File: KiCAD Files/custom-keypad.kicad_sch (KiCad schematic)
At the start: 134 parts, among them SW1 SW_Push, SW10 SW_Push, SW11 SW_Push, SW12 SW_Push, SW13 SW_Push, SW14 SW_Push, SW15 SW_Push, SW16 SW_Push, SW17 SW_Push, SW18 SW_Push, SW19 SW_Push, SW2 SW_Push, SW20 SW_Push, SW21 SW_Push, SW22 SW_Push, SW23 SW_Push, SW24 SW_Push, SW25 SW_Push, SW26 SW_Push, SW27 SW_Push, SW28 SW_Push, SW29 SW_Push, SW3 SW_Push, SW30 SW_Push, SW31 SW_Push, SW32 SW_Push, SW33 SW_Push, SW34 SW_Push, SW35 SW_Push, SW36 SW_Push, SW37 SW_Push, SW38 SW_Push, SW39 SW_Push, SW4 SW_Push, SW40 SW_Push, SW41 SW_Push, SW42 SW_Push, SW43 SW_Push, SW44 SW_Push, SW45 SW_Push, SW46 SW_Push, SW47 SW_Push, SW48 SW_Push, SW49 SW_Push, SW5 SW_Push, SW50 SW_Push, SW51 SW_Push, SW52 SW_Push, SW53 SW_Push, SW54 SW_Push, SW55 SW_Push, SW56 SW_Push, SW57 SW_Push, SW58 SW_Push, SW59 SW_Push, SW6 SW_Push, SW60 SW_Push, SW61 SW_Push, SW62 SW_Push, SW63 SW_Push, SW64 SW_Push, SW65 SW_Push, SW66 SW_Push, SW67 SW_Push, SW7 SW_Push, SW8 SW_Push, SW9 SW_Push

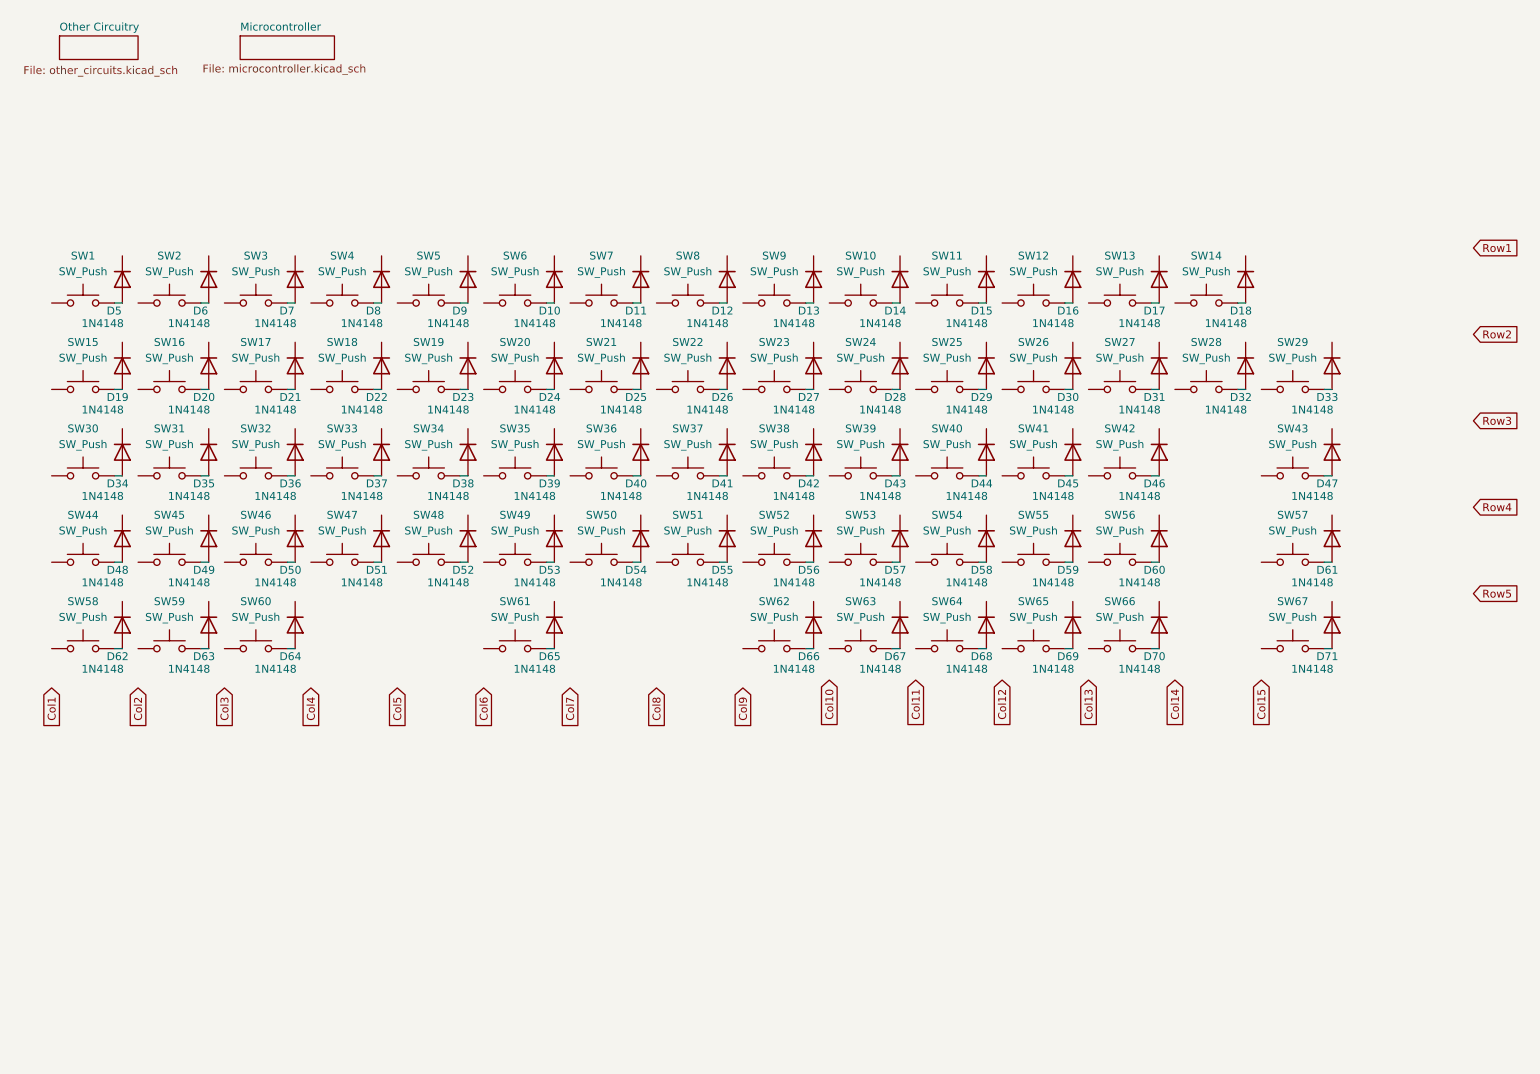
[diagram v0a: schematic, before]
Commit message: Revert "started adjusting changes for 65% keyboard"
This reverts commit 731512e8e337a2e6137dad3074b859df4f5567bd.
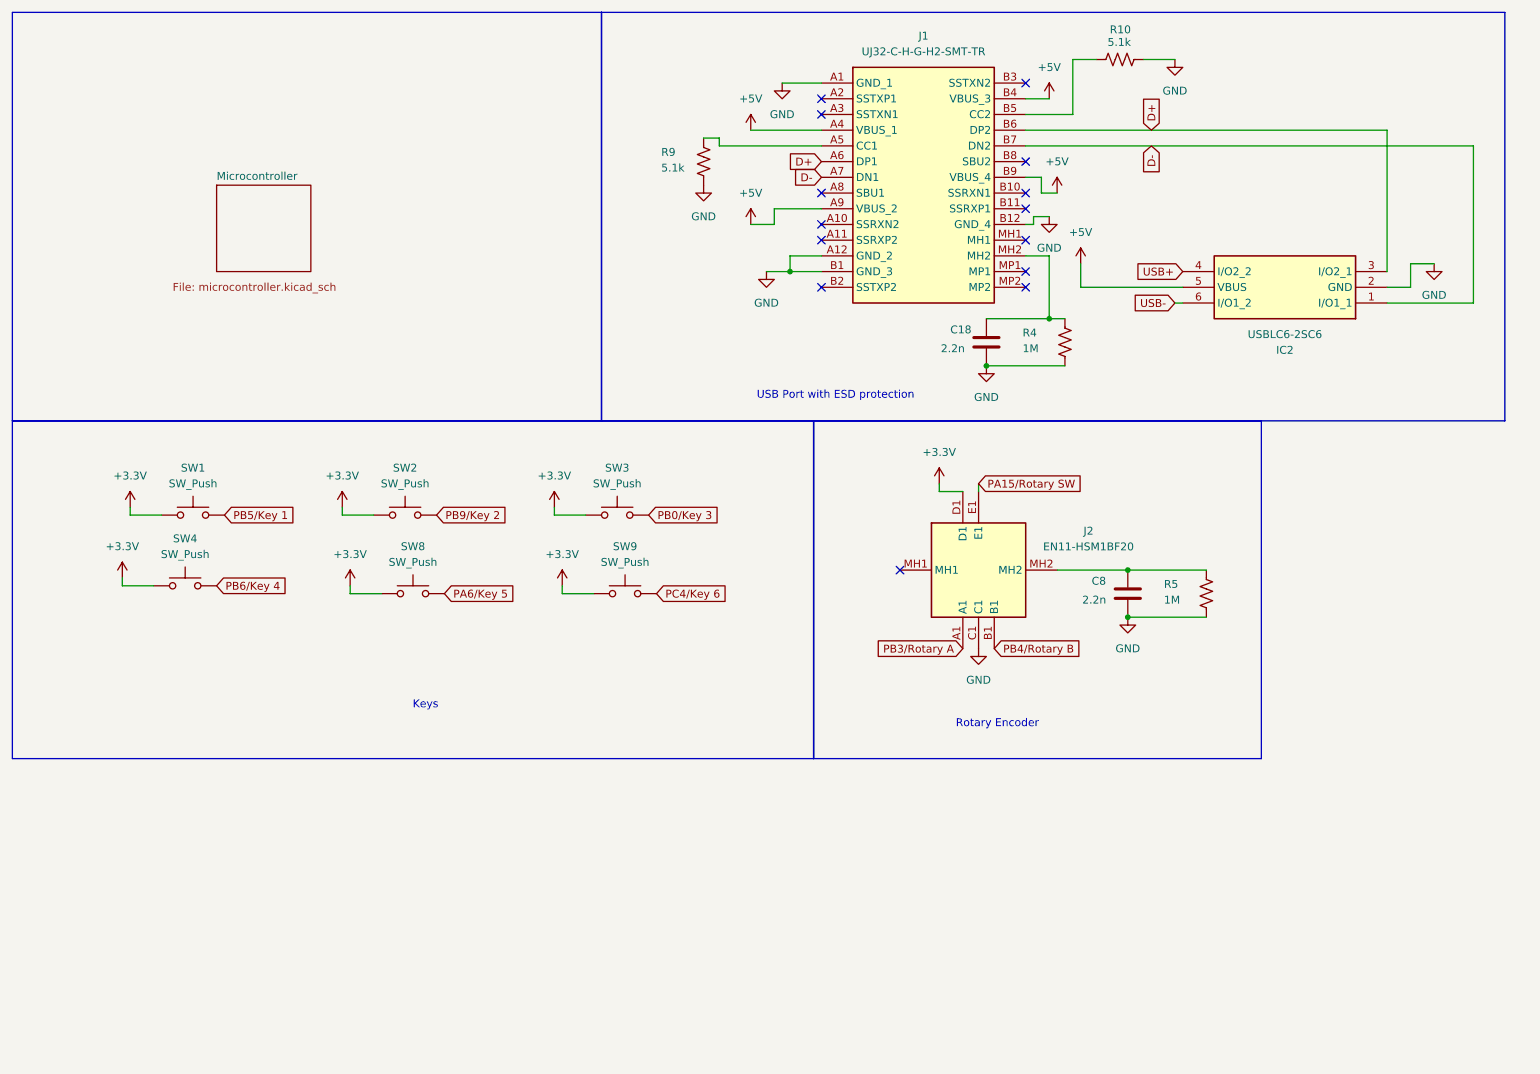
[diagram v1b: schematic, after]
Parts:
- removed D10, D11, D12, D13, D14, D15, D16, D17, D18, D19, D20, D21, D22, D23, D24, D25, D26, D27, D28, D29, D30, D31, D32, D33, D34, D35, D36, D37, D38, D39, D40, D41, D42, D43, D44, D45, D46, D47, D48, D49, D5, D50, D51, D52, D53, D54, D55, D56, D57, D58, D59, D6, D60, D61, D62, D63, D64, D65, D66, D67, D68, D69, D7, D70, D71, D8, D9: 1N4148, Diode_THT:D_DO-35_SOD27_P7.62mm_Horizontal, symbol Diode:1N4148
- removed SW10, SW11, SW12, SW13, SW14, SW15, SW16, SW17, SW18, SW19, SW20, SW21, SW22, SW23, SW24, SW25, SW26, SW27, SW28, SW29, SW30, SW31, SW32, SW33, SW34, SW35, SW36, SW37, SW38, SW39, SW40, SW41, SW42, SW43, SW44, SW45, SW46, SW47, SW48, SW49, SW5, SW50, SW51, SW52, SW53, SW54, SW55, SW56, SW57, SW58, SW59, SW6, SW60, SW61, SW62, SW63, SW64, SW65, SW66, SW67, SW7: SW_Push, symbol Switch:SW_Push
- added C18, C8: 2.2n, Capacitor_SMD:C_0805_2012Metric_Pad1.18x1.45mm_HandSolder, symbol CustomSymbols:C
- added IC2: USBLC6-2SC6, SOT95P280X145-6N, symbol CustomSymbols:USBLC6-2SC6
- added J1: UJ32-C-H-G-H2-SMT-TR, UJ32CHGH2SMTTR, symbol CustomSymbols:UJ32-C-H-G-H2-SMT-TR
- added J2: EN11-HSM1BF20, EN11HSM1BF20, symbol CustomSymbols:EN11-HSM1BF20
- added R10, R9: 5.1k, Resistor_SMD:R_0805_2012Metric_Pad1.20x1.40mm_HandSolder, symbol CustomSymbols:R_US
- added R4, R5: 1M, Resistor_SMD:R_0805_2012Metric_Pad1.20x1.40mm_HandSolder, symbol CustomSymbols:R_US
- SW1, SW2, SW3, SW4, SW8, SW9: footprint (none) -> CustomFootprints:SW_MX
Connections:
- net PC4/Key 6: now reaches SW9.2
- net +3.3V: now reaches SW1.1
- net +3.3V: now also SW2.1, SW3.1, SW4.1, SW8.1, SW9.1, J2.D1
- net PB5/Key 1: now reaches SW1.2
- net PA6/Key 5: now reaches SW8.2
- net PB6/Key 4: now reaches SW4.2
- net PB9/Key 2: now reaches SW2.2
- net PB0/Key 3: now reaches SW3.2
- new net: C18.1, J1.MH2, R4.1
- new net: C8.1, J2.MH2, R5.1
- new net: J1.A5 (CC1), R9.1
- new net: J1.B5 (CC2), R10.1
- new net +5V: IC2.5 (VBUS), J1.A4 (VBUS_1), J1.A9 (VBUS_2), J1.B4 (VBUS_3), J1.B9 (VBUS_4)
- new net D+: IC2.3 (I/O2_1), J1.A6 (DP1), J1.B6 (DP2)
- new net D-: IC2.1 (I/O1_1), J1.A7 (DN1), J1.B7 (DN2)
- new net GND: C18.2, C8.2, IC2.2 (GND), J1.A1 (GND_1), J1.A12 (GND_2), J1.B1 (GND_3), J1.B12 (GND_4), J2.C1, R10.2, R4.2, R5.2, R9.2
- new net PA15/Rotary SW: J2.E1
- new net PB3/Rotary A: J2.A1
- new net PB4/Rotary B: J2.B1
- new net USB+: IC2.4 (I/O2_2)
- new net USB-: IC2.6 (I/O1_2)
- no-connect marks 0 -> 14
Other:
- removed sheet Other Circuitry
- note added: "Keys"
- note added: "Rotary Encoder"
- note added: "USB Port with ESD protection"

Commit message: updated with keyboard 65%
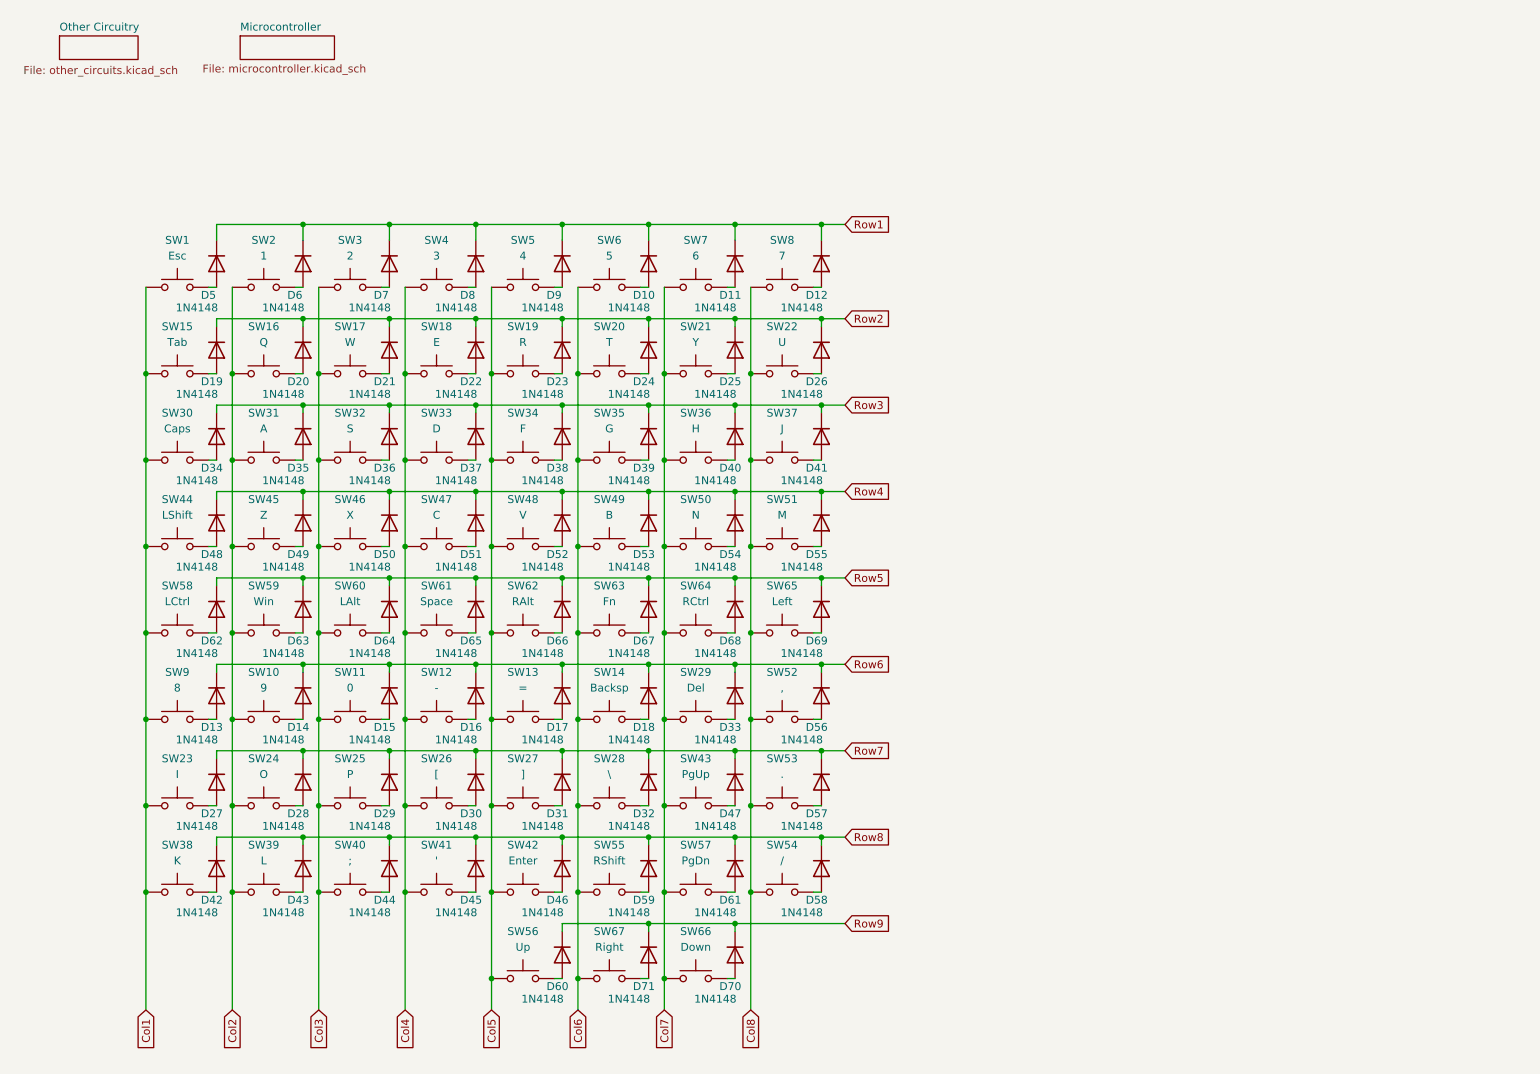
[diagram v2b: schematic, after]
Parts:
- removed C18, C8: 2.2n, Capacitor_SMD:C_0805_2012Metric_Pad1.18x1.45mm_HandSolder, symbol CustomSymbols:C
- removed IC2: USBLC6-2SC6, SOT95P280X145-6N, symbol CustomSymbols:USBLC6-2SC6
- removed J1: UJ32-C-H-G-H2-SMT-TR, UJ32CHGH2SMTTR, symbol CustomSymbols:UJ32-C-H-G-H2-SMT-TR
- removed J2: EN11-HSM1BF20, EN11HSM1BF20, symbol CustomSymbols:EN11-HSM1BF20
- removed R10, R9: 5.1k, Resistor_SMD:R_0805_2012Metric_Pad1.20x1.40mm_HandSolder, symbol CustomSymbols:R_US
- removed R4, R5: 1M, Resistor_SMD:R_0805_2012Metric_Pad1.20x1.40mm_HandSolder, symbol CustomSymbols:R_US
- added D10, D11, D12, D13, D14, D15, D16, D17, D18, D19, D20, D21, D22, D23, D24, D25, D26, D27, D28, D29, D30, D31, D32, D33, D34, D35, D36, D37, D38, D39, D40, D41, D42, D43, D44, D45, D46, D47, D48, D49, D5, D50, D51, D52, D53, D54, D55, D56, D57, D58, D59, D6, D60, D61, D62, D63, D64, D65, D66, D67, D68, D69, D7, D70, D71, D8, D9: 1N4148, Diode_THT:D_DO-35_SOD27_P7.62mm_Horizontal, symbol Diode:1N4148
- added SW10: 9, symbol Switch:SW_Push
- added SW11: 0, symbol Switch:SW_Push
- added SW12: -, symbol Switch:SW_Push
- added SW13: =, symbol Switch:SW_Push
- added SW14: Backsp, symbol Switch:SW_Push
- added SW15: Tab, symbol Switch:SW_Push
- added SW16: Q, symbol Switch:SW_Push
- added SW17: W, symbol Switch:SW_Push
- added SW18: E, symbol Switch:SW_Push
- added SW19: R, symbol Switch:SW_Push
- added SW20: T, symbol Switch:SW_Push
- added SW21: Y, symbol Switch:SW_Push
- added SW22: U, symbol Switch:SW_Push
- added SW23: I, symbol Switch:SW_Push
- added SW24: O, symbol Switch:SW_Push
- added SW25: P, symbol Switch:SW_Push
- added SW26: [, symbol Switch:SW_Push
- added SW27: ], symbol Switch:SW_Push
- added SW28: \, symbol Switch:SW_Push
- added SW29: Del, symbol Switch:SW_Push
- added SW30: Caps, symbol Switch:SW_Push
- added SW31: A, symbol Switch:SW_Push
- added SW32: S, symbol Switch:SW_Push
- added SW33: D, symbol Switch:SW_Push
- added SW34: F, symbol Switch:SW_Push
- added SW35: G, symbol Switch:SW_Push
- added SW36: H, symbol Switch:SW_Push
- added SW37: J, symbol Switch:SW_Push
- added SW38: K, symbol Switch:SW_Push
- added SW39: L, symbol Switch:SW_Push
- added SW40: ;, symbol Switch:SW_Push
- added SW41: ', symbol Switch:SW_Push
- added SW42: Enter, symbol Switch:SW_Push
- added SW43: PgUp, symbol Switch:SW_Push
- added SW44: LShift, symbol Switch:SW_Push
- added SW45: Z, symbol Switch:SW_Push
- added SW46: X, symbol Switch:SW_Push
- added SW47: C, symbol Switch:SW_Push
- added SW48: V, symbol Switch:SW_Push
- added SW49: B, symbol Switch:SW_Push
- added SW5: 4, symbol Switch:SW_Push
- added SW50: N, symbol Switch:SW_Push
- added SW51: M, symbol Switch:SW_Push
- added SW52: ,, symbol Switch:SW_Push
- added SW53: ., symbol Switch:SW_Push
- added SW54: /, symbol Switch:SW_Push
- added SW55: RShift, symbol Switch:SW_Push
- added SW56: Up, symbol Switch:SW_Push
- added SW57: PgDn, symbol Switch:SW_Push
- added SW58: LCtrl, symbol Switch:SW_Push
- added SW59: Win, symbol Switch:SW_Push
- added SW6: 5, symbol Switch:SW_Push
- added SW60: LAlt, symbol Switch:SW_Push
- added SW61: Space, symbol Switch:SW_Push
- added SW62: RAlt, symbol Switch:SW_Push
- added SW63: Fn, symbol Switch:SW_Push
- added SW64: RCtrl, symbol Switch:SW_Push
- added SW65: Left, symbol Switch:SW_Push
- added SW66: Down, symbol Switch:SW_Push
- added SW67: Right, symbol Switch:SW_Push
- added SW7: 6, symbol Switch:SW_Push
- SW1: value SW_Push -> Esc; footprint CustomFootprints:SW_MX -> (none)
- SW2: value SW_Push -> 1; footprint CustomFootprints:SW_MX -> (none)
- SW3: value SW_Push -> 2; footprint CustomFootprints:SW_MX -> (none)
- SW4: value SW_Push -> 3; footprint CustomFootprints:SW_MX -> (none)
- SW8: value SW_Push -> 7; footprint CustomFootprints:SW_MX -> (none)
- SW9: value SW_Push -> 8; footprint CustomFootprints:SW_MX -> (none)
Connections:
- removed net +3.3V: SW1.1, SW2.1, SW3.1, SW4.1, SW8.1, SW9.1
- net PA6/Key 5: no longer names the net of SW8.2
- net PA6/Key 5: now also D12.2 (A)
- net PB0/Key 3: no longer names the net of SW3.2
- net PB0/Key 3: now also D7.2 (A)
- net PB5/Key 1: no longer names the net of SW1.2
- net PB5/Key 1: now also D5.2 (A)
- net PB6/Key 4: no longer names the net of SW4.2
- net PB6/Key 4: now also D8.2 (A)
- net PB9/Key 2: no longer names the net of SW2.2
- net PB9/Key 2: now also D6.2 (A)
- net PC4/Key 6: no longer names the net of SW9.2
- net PC4/Key 6: now also D13.2 (A)
- new net: D14.2 (A), SW10.2
- new net: D22.2 (A), SW18.2
- new net: D27.2 (A), SW23.2
- new net: D49.2 (A), SW45.2
- new net: D33.2 (A), SW29.2
- new net: D37.2 (A), SW33.2
- new net: D62.2 (A), SW58.2
- new net: D43.2 (A), SW39.2
- new net: D17.2 (A), SW13.2
- new net: D52.2 (A), SW48.2
- new net: D54.2 (A), SW50.2
- new net: D63.2 (A), SW59.2
- new net: D34.2 (A), SW30.2
- new net: D36.2 (A), SW32.2
- new net: D59.2 (A), SW55.2
- new net: D46.2 (A), SW42.2
- new net: D24.2 (A), SW20.2
- new net: D23.2 (A), SW19.2
- new net: D42.2 (A), SW38.2
- new net: D56.2 (A), SW52.2
- new net: D44.2 (A), SW40.2
- new net: D47.2 (A), SW43.2
- new net: D50.2 (A), SW46.2
- new net: D18.2 (A), SW14.2
- new net: D51.2 (A), SW47.2
- new net: D67.2 (A), SW63.2
- new net: D60.2 (A), SW56.2
- new net: D15.2 (A), SW11.2
- new net: D70.2 (A), SW66.2
- new net: D45.2 (A), SW41.2
- new net: D58.2 (A), SW54.2
- new net: D40.2 (A), SW36.2
- new net: D57.2 (A), SW53.2
- new net: D30.2 (A), SW26.2
- new net: D48.2 (A), SW44.2
- new net: D71.2 (A), SW67.2
- new net: D11.2 (A), SW7.2
- new net: D25.2 (A), SW21.2
- new net: D19.2 (A), SW15.2
- new net: D41.2 (A), SW37.2
- new net: D64.2 (A), SW60.2
- new net: D16.2 (A), SW12.2
- new net: D65.2 (A), SW61.2
- new net: D68.2 (A), SW64.2
- new net: D66.2 (A), SW62.2
- new net: D39.2 (A), SW35.2
- new net: D69.2 (A), SW65.2
- new net: D29.2 (A), SW25.2
- new net: D55.2 (A), SW51.2
- new net: D21.2 (A), SW17.2
- new net: D26.2 (A), SW22.2
- new net: D31.2 (A), SW27.2
- new net: D28.2 (A), SW24.2
- new net: D9.2 (A), SW5.2
- new net: D32.2 (A), SW28.2
- new net: D35.2 (A), SW31.2
- new net: D10.2 (A), SW6.2
- new net: D38.2 (A), SW34.2
- new net: D20.2 (A), SW16.2
- new net: D61.2 (A), SW57.2
- new net: D53.2 (A), SW49.2
- new net Col1: SW1.1, SW15.1, SW23.1, SW30.1, SW38.1, SW44.1, SW58.1, SW9.1
- new net Col2: SW10.1, SW16.1, SW2.1, SW24.1, SW31.1, SW39.1, SW45.1, SW59.1
- new net Col3: SW11.1, SW17.1, SW25.1, SW3.1, SW32.1, SW40.1, SW46.1, SW60.1
- new net Col4: SW12.1, SW18.1, SW26.1, SW33.1, SW4.1, SW41.1, SW47.1, SW61.1
- new net Col5: SW13.1, SW19.1, SW27.1, SW34.1, SW42.1, SW48.1, SW5.1, SW56.1, SW62.1
- new net Col6: SW14.1, SW20.1, SW28.1, SW35.1, SW49.1, SW55.1, SW6.1, SW63.1, SW67.1
- new net Col7: SW21.1, SW29.1, SW36.1, SW43.1, SW50.1, SW57.1, SW64.1, SW66.1, SW7.1
- new net Col8: SW22.1, SW37.1, SW51.1, SW52.1, SW53.1, SW54.1, SW65.1, SW8.1
- new net Row1: D10.1 (K), D11.1 (K), D12.1 (K), D5.1 (K), D6.1 (K), D7.1 (K), D8.1 (K), D9.1 (K)
- new net Row2: D19.1 (K), D20.1 (K), D21.1 (K), D22.1 (K), D23.1 (K), D24.1 (K), D25.1 (K), D26.1 (K)
- new net Row3: D34.1 (K), D35.1 (K), D36.1 (K), D37.1 (K), D38.1 (K), D39.1 (K), D40.1 (K), D41.1 (K)
- new net Row4: D48.1 (K), D49.1 (K), D50.1 (K), D51.1 (K), D52.1 (K), D53.1 (K), D54.1 (K), D55.1 (K)
- new net Row5: D62.1 (K), D63.1 (K), D64.1 (K), D65.1 (K), D66.1 (K), D67.1 (K), D68.1 (K), D69.1 (K)
- new net Row6: D13.1 (K), D14.1 (K), D15.1 (K), D16.1 (K), D17.1 (K), D18.1 (K), D33.1 (K), D56.1 (K)
- new net Row7: D27.1 (K), D28.1 (K), D29.1 (K), D30.1 (K), D31.1 (K), D32.1 (K), D47.1 (K), D57.1 (K)
- new net Row8: D42.1 (K), D43.1 (K), D44.1 (K), D45.1 (K), D46.1 (K), D58.1 (K), D59.1 (K), D61.1 (K)
- new net Row9: D60.1 (K), D70.1 (K), D71.1 (K)
- no-connect marks 14 -> 0
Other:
- added sheet Other Circuitry (other_circuits.kicad_sch)
- note removed: "Keys"
- note removed: "Rotary Encoder"
- note removed: "USB Port with ESD protection"
